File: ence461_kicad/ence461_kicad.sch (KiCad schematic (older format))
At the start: 57 parts, among them Q1 Q_PMOS_GSD, U1 LMV324, U2 LMV324, U3 LMV324, U4 74HC3G14DP, U5 LMV321, U6 NCV7344D13R2GOSCT-ND, U7 TPS717DRV-WSON, U8 TPS71433DRVR

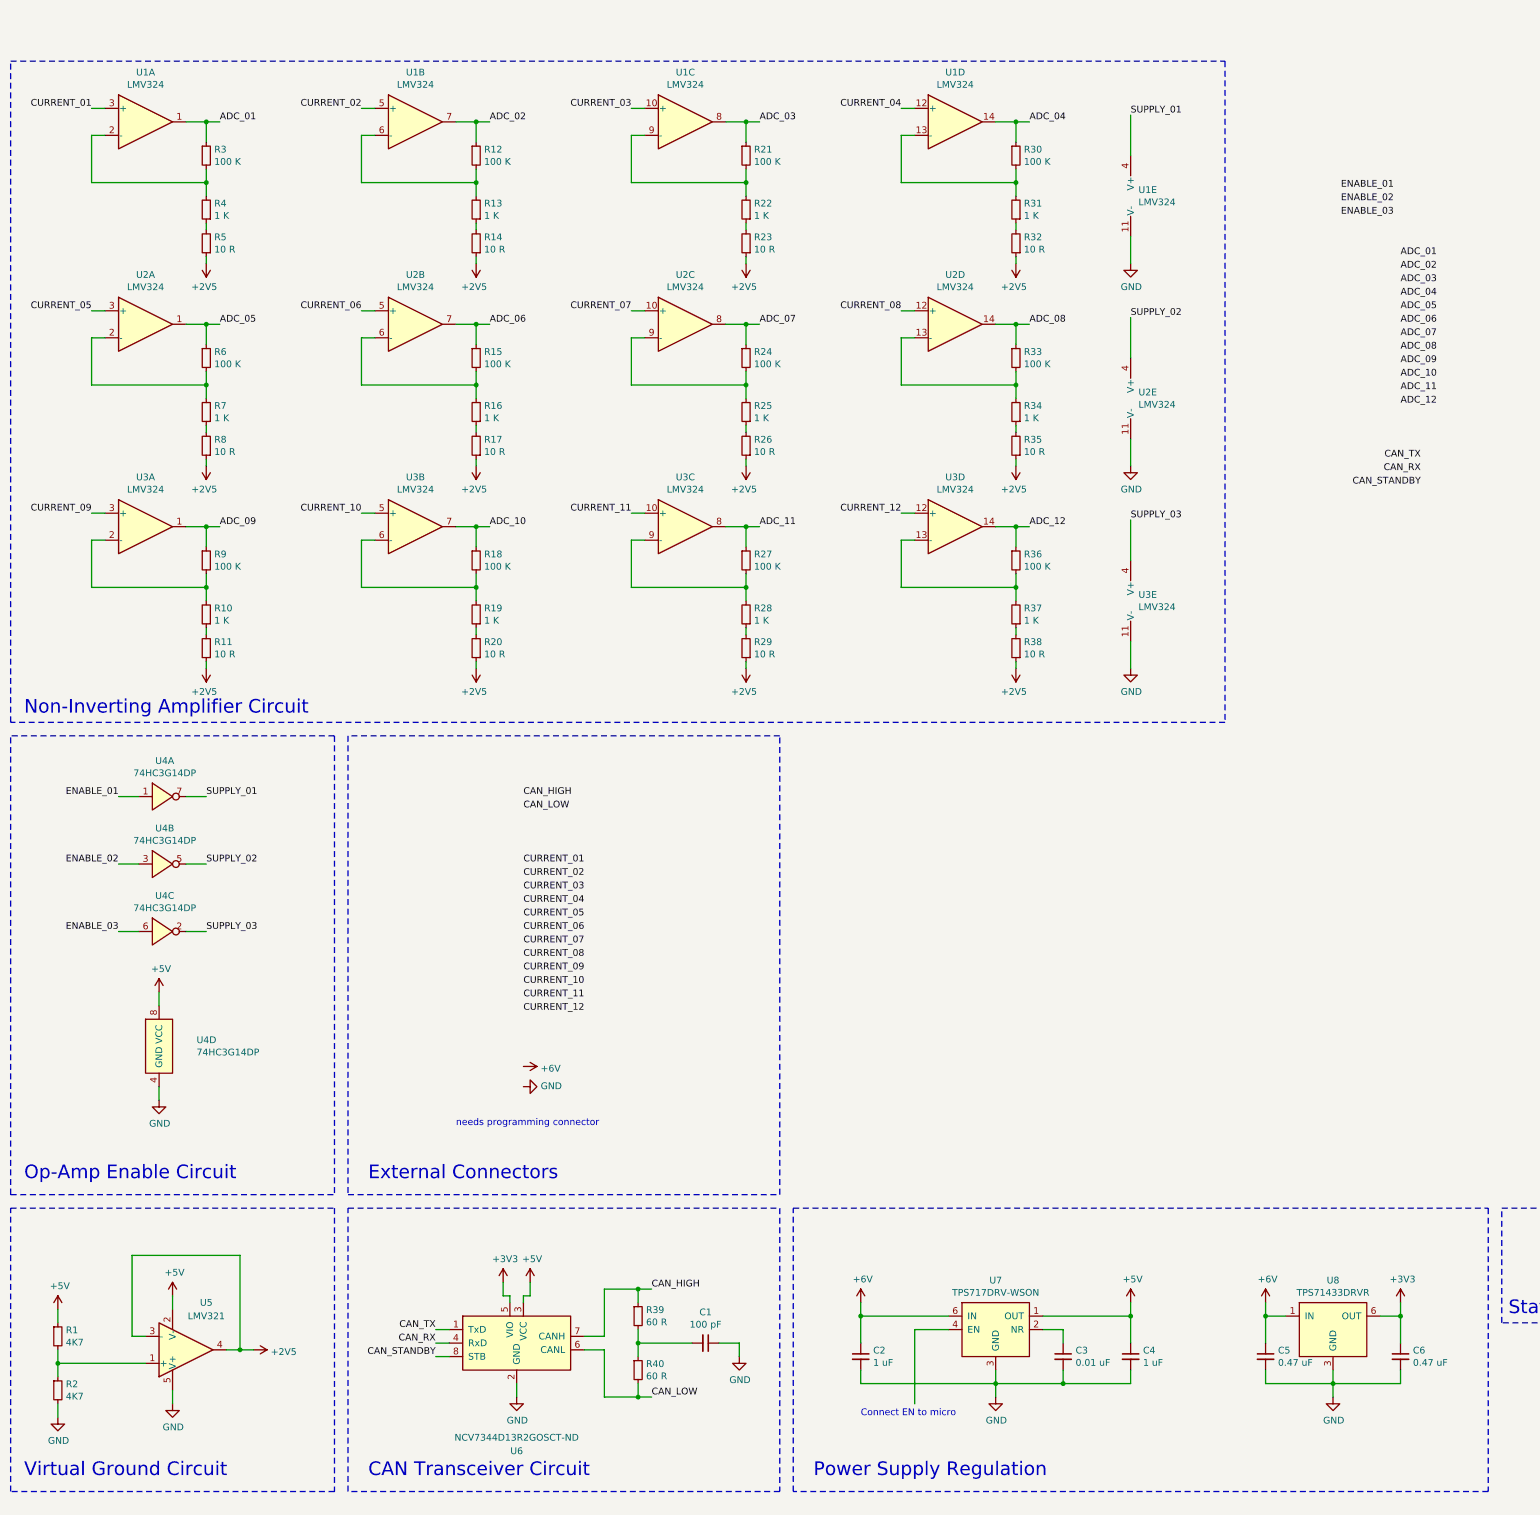
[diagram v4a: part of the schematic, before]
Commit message: Added micro to schematic. Laid out.
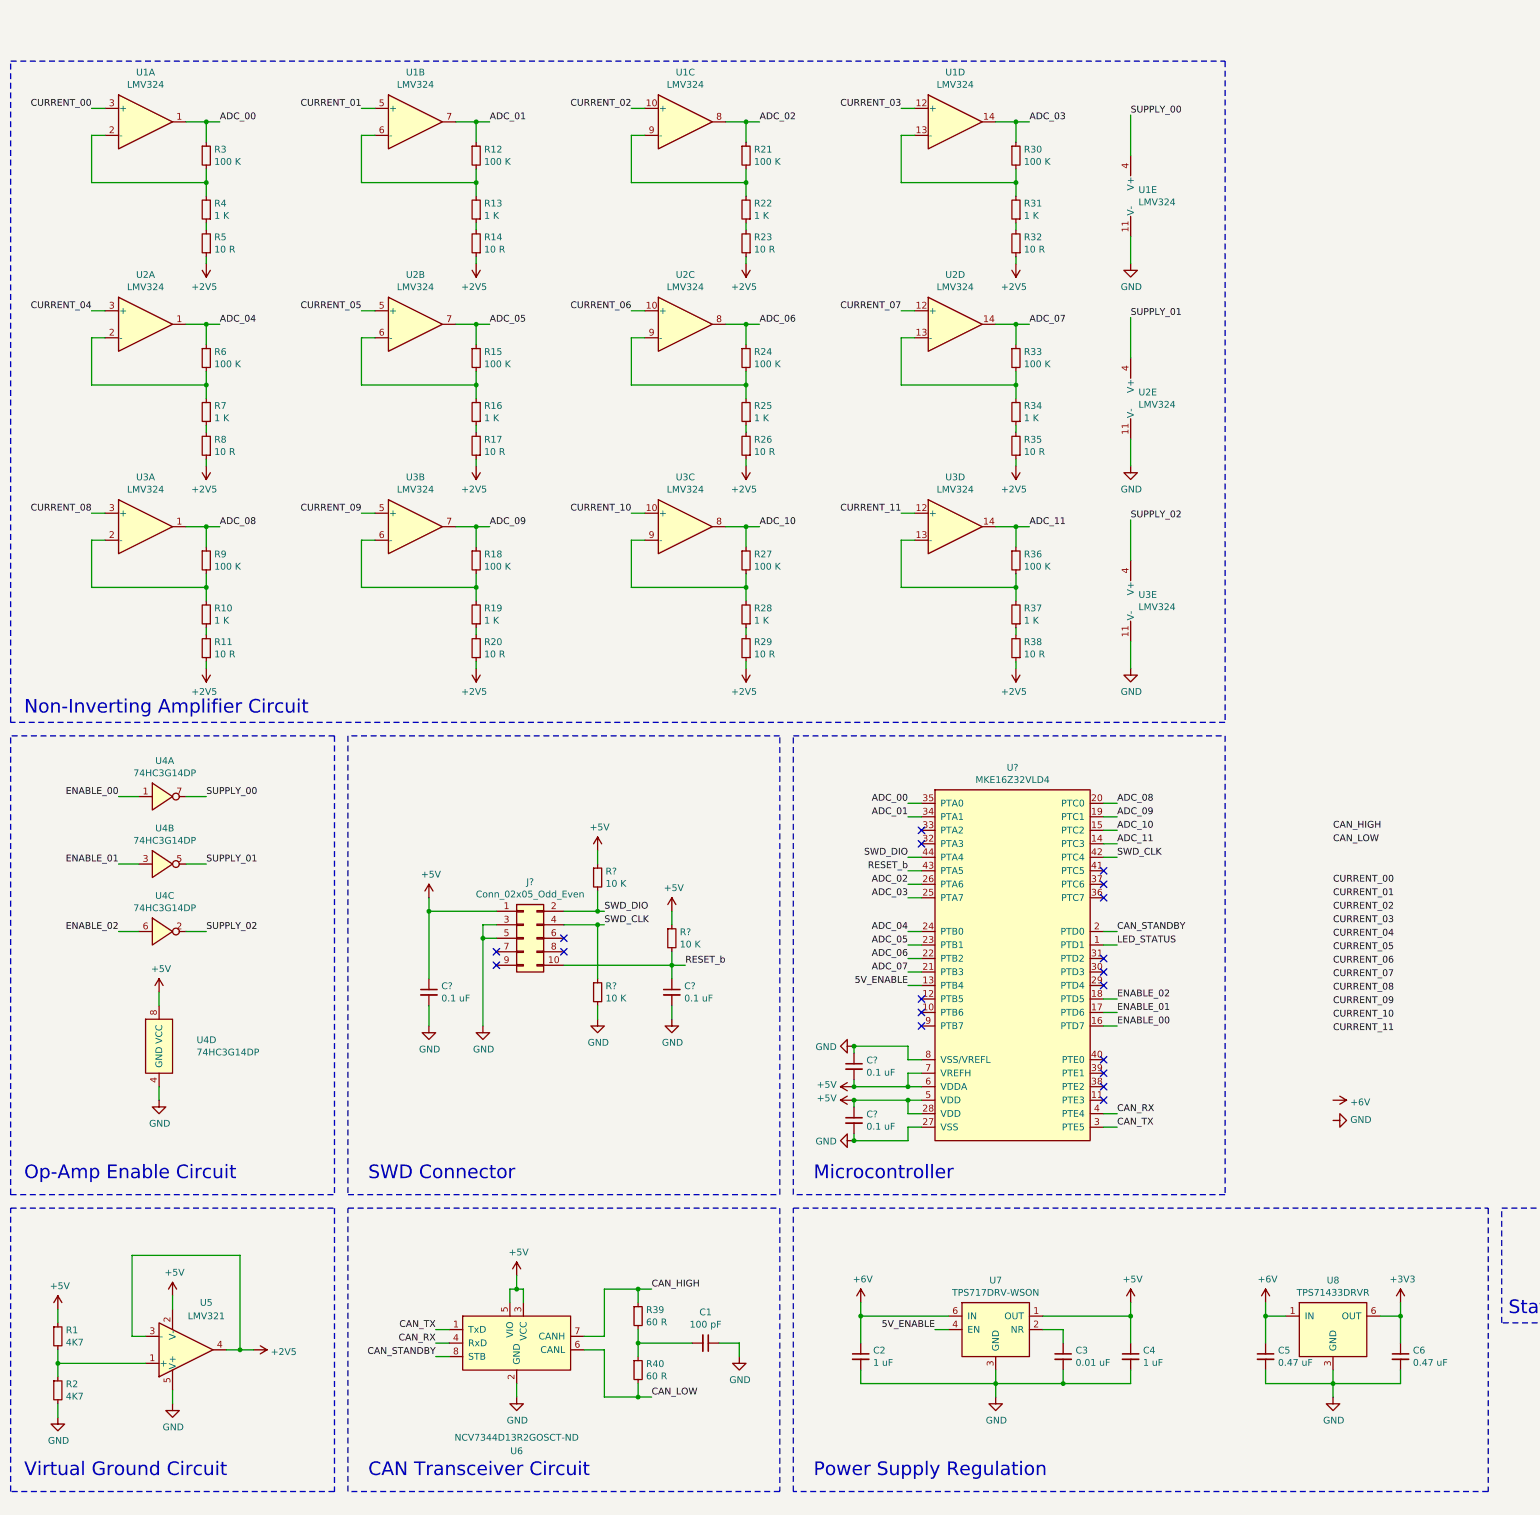
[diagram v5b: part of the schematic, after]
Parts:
- added C? (x4): 0.1 uF, symbol Device:C_Small
- added J?: Conn_02x05_Odd_Even, symbol Connector_Generic:Conn_02x05_Odd_Even
- added R? (x3): 10 K, symbol Device:R_Small
- added U?: MKE16Z32VLD4, Package_QFP:LQFP-44_10x10mm_P0.8mm, symbol ence461_symbol_library:MKE16Z32VLD4
- R39, R40: Comment (none) -> DNF
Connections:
- net ADC_12 is gone; now on net ADC_11: R36.1, U3.14
- net CURRENT_12 is gone; now on net CURRENT_11: U3.12 (+)
- net ENABLE_03 is gone; now on net ENABLE_02: U4.6
- net SUPPLY_03 is gone; now on net SUPPLY_02: U3.4 (V+), U4.2
- net +3V3: no longer U6.5 (VIO)
- net +5V: now also U6.5 (VIO), C?.1, C?.1, C?.2, J?.1 (Pin_1), R?.1, R?.1, U?.28 (VDD), U?.5 (VDD), U?.6 (VDDA), U?.7 (VREFH)
- net ADC_01: now also R12.1, U1.7, U?.34 (PTA1); no longer R3.1, U1.1
- net ADC_02: now also R21.1, U1.8, U?.26 (PTA6); no longer R12.1, U1.7
- net ADC_03: now also R30.1, U1.14, U?.25 (PTA7); no longer R21.1, U1.8
- net ADC_04: now also R6.1, U2.1, U?.24 (PTB0); no longer R30.1, U1.14
- net ADC_05: now also R15.1, U2.7, U?.23 (PTB1); no longer R6.1, U2.1
- net ADC_06: now also R24.1, U2.8, U?.22 (PTB2); no longer R15.1, U2.7
- net ADC_07: now also R33.1, U2.14, U?.21 (PTB3); no longer R24.1, U2.8
- net ADC_08: now also R9.1, U3.1, U?.20 (PTC0); no longer R33.1, U2.14
- net ADC_09: now also R18.1, U3.7, U?.19 (PTC1); no longer R9.1, U3.1
- net ADC_10: now also R27.1, U3.8, U?.15 (PTC2); no longer R18.1, U3.7
- net ADC_11: now also U?.14 (PTC3); no longer R27.1, U3.8
- net CAN_RX: now also U?.4 (PTE4)
- net CAN_STANDBY: now also U?.2 (PTD0)
- net CAN_TX: now also U?.3 (PTE5)
- net CURRENT_01: now also U1.5 (+); no longer U1.3 (+)
- net CURRENT_02: now also U1.10 (+); no longer U1.5 (+)
- net CURRENT_03: now also U1.12 (+); no longer U1.10 (+)
- net CURRENT_04: now also U2.3 (+); no longer U1.12 (+)
- net CURRENT_05: now also U2.5 (+); no longer U2.3 (+)
- net CURRENT_06: now also U2.10 (+); no longer U2.5 (+)
- net CURRENT_07: now also U2.12 (+); no longer U2.10 (+)
- net CURRENT_08: now also U3.3 (+); no longer U2.12 (+)
- net CURRENT_09: now also U3.5 (+); no longer U3.3 (+)
- net CURRENT_10: now also U3.10 (+); no longer U3.5 (+)
- net CURRENT_11: no longer U3.10 (+)
- net ENABLE_01: now also U4.3, U?.17 (PTD6); no longer U4.1
- net ENABLE_02: now also U?.18 (PTD5); no longer U4.3
- net GND: now also C?.1, C?.2, C?.2, C?.2, J?.3 (Pin_3), J?.5 (Pin_5), R?.2, U?.27 (VSS), U?.8 (VSS/VREFL)
- net LED_STATUS: now also U?.1 (PTD1)
- net SUPPLY_01: now also U2.4 (V+), U4.5; no longer U1.4 (V+), U4.7
- net SUPPLY_02: no longer U2.4 (V+), U4.5
- net 5V_ENABLE: now reaches U7.4 (EN)
- net 5V_ENABLE: now also U?.13 (PTB4)
- new net ADC_00: R3.1, U1.1, U?.35 (PTA0)
- new net CURRENT_00: U1.3 (+)
- new net ENABLE_00: U4.1, U?.16 (PTD7)
- new net RESET_b: C?.1, J?.10 (Pin_10), R?.2, U?.43 (PTA5)
- new net SUPPLY_00: U1.4 (V+), U4.7
- new net SWD_CLK: J?.4 (Pin_4), R?.1, U?.42 (PTC4)
- new net SWD_DIO: J?.2 (Pin_2), R?.2, U?.44 (PTA4)
- no-connect marks 0 -> 19
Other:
- note added: "Microcontroller"
- note added: "SWD Connector"
- note removed: "Connect EN to micro"
- note removed: "External Connectors"
- note removed: "needs programming connector"

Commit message: Forgot to save.
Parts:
- C10, C7, C8, C9: renamed from C?; footprint (none) -> Capacitor_SMD:C_0603_1608Metric
- J1: renamed from J?; footprint (none) -> Connector_PinHeader_1.27mm:PinHeader_2x05_P1.27mm_Vertical
- R42, R43, R44: renamed from R?; footprint (none) -> Resistor_SMD:R_0603_1608Metric
- gave numbers to parts that had none: 1
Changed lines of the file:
@@
 5V_ENABLE
 $Comp
-L ence461_symbol_library:MKE16Z32VLD4 U?
+L ence461_symbol_library:MKE16Z32VLD4 U9
 U 1 1 5EF406AC
 P 8150 7500
-F 0 "U?" H 8125 9215 50  0000 C CNN
+F 0 "U9" H 8125 9215 50  0000 C CNN
 F 1 "MKE16Z32VLD4" H 8125 9124 50  0000 C CNN
 F 2 "Package_QFP:LQFP-44_10x10mm_P0.8mm" H 8150 7500 50  0001 C CNN
@@
 $EndComp
 $Comp
-L power:GND #PWR?
+L power:GND #PWR0101
 U 1 1 5F0030BB
 P 6950 8550
-F 0 "#PWR?" H 6950 8300 50  0001 C CNN
+F 0 "#PWR0101" H 6950 8300 50  0001 C CNN
 F 1 "GND" V 6955 8422 50  0000 R CNN
 F 2 "" H 6950 8550 50  0001 C CNN
@@
 $EndComp
 $Comp
-L power:+5V #PWR?
+L power:+5V #PWR0102
 U 1 1 5F0101F7
 P 6950 8250
-F 0 "#PWR?" H 6950 8100 50  0001 C CNN
+F 0 "#PWR0102" H 6950 8100 50  0001 C CNN
 F 1 "+5V" V 6965 8378 50  0000 L CNN
 F 2 "" H 6950 8250 50  0001 C CNN
@@
 	7350 7300 7450 7300
 $Comp
-L Device:C_Small C?
+L Device:C_Small C10
 U 1 1 5F0E4CD6
 P 6950 8400
-F 0 "C?" H 7042 8446 50  0000 L CNN
+F 0 "C10" H 7042 8446 50  0000 L CNN
 F 1 "0.1 uF" H 7042 8355 50  0000 L CNN
-F 2 "" H 6950 8400 50  0001 C CNN
+F 2 "Capacitor_SMD:C_0603_1608Metric" H 6950 8400 50  0001 C CNN
 F 3 "~" H 6950 8400 50  0001 C CNN
 	1    6950 8400
@@
 $EndComp
 $Comp
-L Device:C_Small C?
+L Device:C_Small C9
 U 1 1 5F0E531E
 P 6950 8000
-F 0 "C?" H 7042 8046 50  0000 L CNN
+F 0 "C9" H 7042 8046 50  0000 L CNN
 F 1 "0.1 uF" H 7042 7955 50  0000 L CNN
-F 2 "" H 6950 8000 50  0001 C CNN
+F 2 "Capacitor_SMD:C_0603_1608Metric" H 6950 8000 50  0001 C CNN
 F 3 "~" H 6950 8000 50  0001 C CNN
 	1    6950 8000
@@
 	7350 7950 7450 7950
 $Comp
-L power:+5V #PWR?
+L power:+5V #PWR0103
 U 1 1 5F19BED0
 P 6950 8150
-F 0 "#PWR?" H 6950 8000 50  0001 C CNN
+F 0 "#PWR0103" H 6950 8000 50  0001 C CNN
 F 1 "+5V" V 6965 8278 50  0000 L CNN
 F 2 "" H 6950 8150 50  0001 C CNN
@@
 Connection ~ 6950 8150
 $Comp
-L power:GND #PWR?
+L power:GND #PWR0104
 U 1 1 5F19C444
 P 6950 7850
-F 0 "#PWR?" H 6950 7600 50  0001 C CNN
+F 0 "#PWR0104" H 6950 7600 50  0001 C CNN
 F 1 "GND" V 6955 7722 50  0000 R CNN
 F 2 "" H 6950 7850 50  0001 C CNN
@@
 RESET_b
 $Comp
-L Device:C_Small C?
+L Device:C_Small C8
 U 1 1 5F24DE0C
 P 5600 7450
-F 0 "C?" H 5692 7496 50  0000 L CNN
+F 0 "C8" H 5692 7496 50  0000 L CNN
 F 1 "0.1 uF" H 5692 7405 50  0000 L CNN
-F 2 "" H 5600 7450 50  0001 C CNN
+F 2 "Capacitor_SMD:C_0603_1608Metric" H 5600 7450 50  0001 C CNN
 F 3 "~" H 5600 7450 50  0001 C CNN
 	1    5600 7450
@@
 $EndComp
 $Comp
-L Device:R_Small R?
+L Device:R_Small R44
 U 1 1 5F24E218
 P 5600 7050
-F 0 "R?" H 5659 7096 50  0000 L CNN
+F 0 "R44" H 5659 7096 50  0000 L CNN
 F 1 "10 K" H 5659 7005 50  0000 L CNN
-F 2 "" H 5600 7050 50  0001 C CNN
+F 2 "Resistor_SMD:R_0603_1608Metric" H 5600 7050 50  0001 C CNN
 F 3 "~" H 5600 7050 50  0001 C CNN
 	1    5600 7050
@@
 $EndComp
 $Comp
-L power:GND #PWR?
+L power:GND #PWR0105
 U 1 1 5F24E975
 P 5600 7650
-F 0 "#PWR?" H 5600 7400 50  0001 C CNN
+F 0 "#PWR0105" H 5600 7400 50  0001 C CNN
 F 1 "GND" H 5605 7477 50  0000 C CNN
 F 2 "" H 5600 7650 50  0001 C CNN
@@
 	5600 7550 5600 7650
 $Comp
-L Connector_Generic:Conn_02x05_Odd_Even J?
+L Connector_Generic:Conn_02x05_Odd_Even J1
 U 1 1 5F2B6500
 P 4500 7050
-F 0 "J?" H 4550 7467 50  0000 C CNN
+F 0 "J1" H 4550 7467 50  0000 C CNN
 F 1 "Conn_02x05_Odd_Even" H 4550 7376 50  0000 C CNN
-F 2 "" H 4500 7050 50  0001 C CNN
+F 2 "Connector_PinHeader_1.27mm:PinHeader_2x05_P1.27mm_Vertical" H 4500 7050 50  0001 C CNN
 F 3 "~" H 4500 7050 50  0001 C CNN
 	1    4500 7050
@@
 $EndComp
 $Comp
-L Device:C_Small C?
+L Device:C_Small C7
 U 1 1 5F2B6C6B
 P 3800 7450
-F 0 "C?" H 3892 7496 50  0000 L CNN
+F 0 "C7" H 3892 7496 50  0000 L CNN
 F 1 "0.1 uF" H 3892 7405 50  0000 L CNN
-F 2 "" H 3800 7450 50  0001 C CNN
+F 2 "Capacitor_SMD:C_0603_1608Metric" H 3800 7450 50  0001 C CNN
 F 3 "~" H 3800 7450 50  0001 C CNN
 	1    3800 7450
@@
 $EndComp
 $Comp
-L Device:R_Small R?
+L Device:R_Small R42
 U 1 1 5F2B7252
 P 5050 6600
-F 0 "R?" H 5109 6646 50  0000 L CNN
+F 0 "R42" H 5109 6646 50  0000 L CNN
 F 1 "10 K" H 5109 6555 50  0000 L CNN
-F 2 "" H 5050 6600 50  0001 C CNN
+F 2 "Resistor_SMD:R_0603_1608Metric" H 5050 6600 50  0001 C CNN
 F 3 "~" H 5050 6600 50  0001 C CNN
 	1    5050 6600
@@
 $EndComp
 $Comp
-L Device:R_Small R?
+L Device:R_Small R43
 U 1 1 5F2B75EC
 P 5050 7450
-F 0 "R?" H 5109 7496 50  0000 L CNN
+F 0 "R43" H 5109 7496 50  0000 L CNN
 F 1 "10 K" H 5109 7405 50  0000 L CNN
-F 2 "" H 5050 7450 50  0001 C CNN
+F 2 "Resistor_SMD:R_0603_1608Metric" H 5050 7450 50  0001 C CNN
 F 3 "~" H 5050 7450 50  0001 C CNN
 	1    5050 7450
@@
 	5600 6850 5600 6950
 $Comp
-L power:+5V #PWR?
+L power:+5V #PWR0106
 U 1 1 5F24E5BB
 P 5600 6850
-F 0 "#PWR?" H 5600 6700 50  0001 C CNN
+F 0 "#PWR0106" H 5600 6700 50  0001 C CNN
 F 1 "+5V" H 5615 7023 50  0000 C CNN
 F 2 "" H 5600 6850 50  0001 C CNN
@@
 $EndComp
 $Comp
-L power:+5V #PWR?
+L power:+5V #PWR0107
 U 1 1 5F35EE5C
 P 5050 6400
-F 0 "#PWR?" H 5050 6250 50  0001 C CNN
+F 0 "#PWR0107" H 5050 6250 50  0001 C CNN
 F 1 "+5V" H 5065 6573 50  0000 C CNN
 F 2 "" H 5050 6400 50  0001 C CNN
@@
 	5050 6400 5050 6500
 $Comp
-L power:GND #PWR?
+L power:GND #PWR0108
 U 1 1 5F36F8DD
 P 5050 7650
-F 0 "#PWR?" H 5050 7400 50  0001 C CNN
+F 0 "#PWR0108" H 5050 7400 50  0001 C CNN
 F 1 "GND" H 5055 7477 50  0000 C CNN
 F 2 "" H 5050 7650 50  0001 C CNN
@@
 	4200 6950 4300 6950
 $Comp
-L power:GND #PWR?
+L power:GND #PWR0109
 U 1 1 5F403E90
 P 4200 7700
-F 0 "#PWR?" H 4200 7450 50  0001 C CNN
+F 0 "#PWR0109" H 4200 7450 50  0001 C CNN
 F 1 "GND" H 4205 7527 50  0000 C CNN
 F 2 "" H 4200 7700 50  0001 C CNN
@@
 Connection ~ 4200 7050
 $Comp
-L power:GND #PWR?
+L power:GND #PWR0110
 U 1 1 5F4179B9
 P 3800 7700
-F 0 "#PWR?" H 3800 7450 50  0001 C CNN
+F 0 "#PWR0110" H 3800 7450 50  0001 C CNN
 F 1 "GND" H 3805 7527 50  0000 C CNN
 F 2 "" H 3800 7700 50  0001 C CNN
@@
 	3800 6850 4300 6850
 $Comp
-L power:+5V #PWR?
+L power:+5V #PWR0111
 U 1 1 5F439FDF
 P 3800 6750
-F 0 "#PWR?" H 3800 6600 50  0001 C CNN
+F 0 "#PWR0111" H 3800 6600 50  0001 C CNN
 F 1 "+5V" H 3815 6923 50  0000 C CNN
 F 2 "" H 3800 6750 50  0001 C CNN
